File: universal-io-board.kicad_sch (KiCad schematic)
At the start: 34 parts, among them J1 Conn_01x03_Pin, J2 Conn_01x22_Socket, J3 Conn_01x22_Socket, J4 Conn_01x02, U1 R-78E5.0-1.0, U2 AMS1117-3.3, U3 ADS1256IDBT, U4 REF5050IDGK, Y1 Crystal

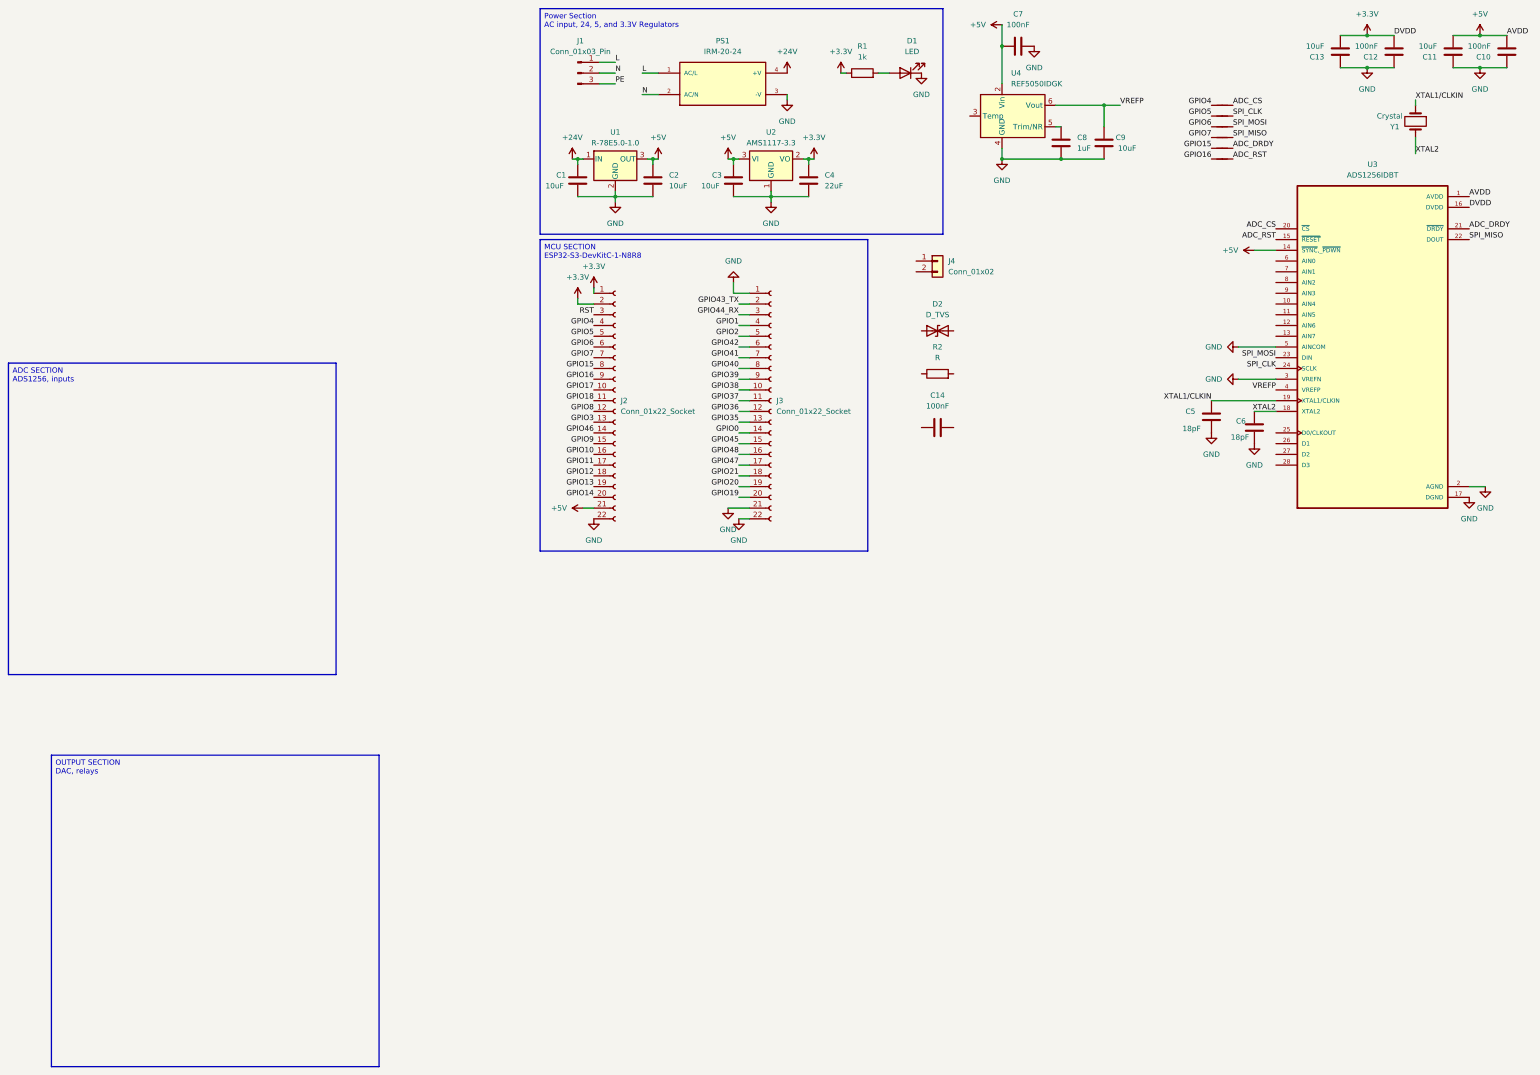
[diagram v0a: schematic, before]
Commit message: Updated schematic and PCB
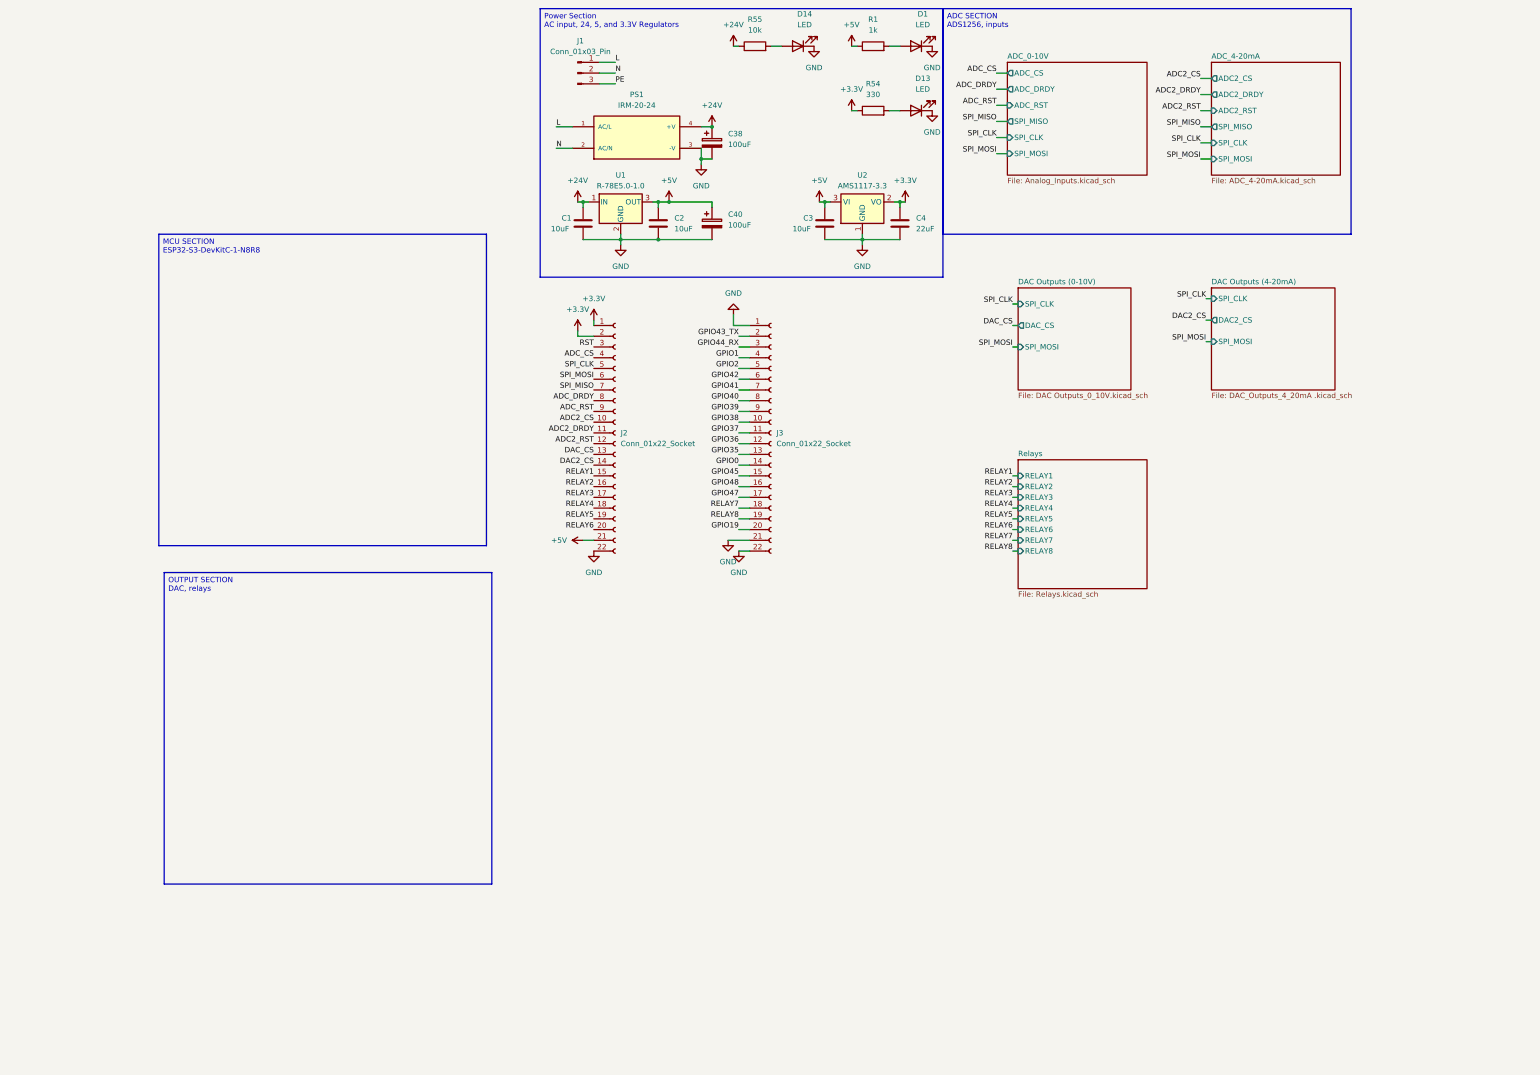
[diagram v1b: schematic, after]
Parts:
- removed C10, C12, C14, C7: 100nF, Capacitor_SMD:C_0805_2012Metric, symbol Device:C
- removed C11, C13, C9: 10uF, Capacitor_SMD:C_0805_2012Metric, symbol Device:C
- removed C5, C6: 18pF, Capacitor_SMD:C_0805_2012Metric, symbol Device:C
- removed C8: 1uF, Capacitor_SMD:C_0805_2012Metric, symbol Device:C
- removed D2: D_TVS, symbol Device:D_TVS
- removed J4: Conn_01x02, symbol Connector_Generic:Conn_01x02
- removed NT1, NT2, NT3, NT4, NT5, NT6: NetTie_2, symbol Device:NetTie_2
- removed R2: R, symbol Device:R
- removed U3: ADS1256IDBT, ADS1256IDBT:SOP65P780X200-28N, symbol ADS1256IDBT:ADS1256IDBT
- removed U4: REF5050IDGK, Package_SO:MSOP-8_3x3mm_P0.65mm, symbol Reference_Voltage:REF5050IDGK
- removed Y1: Crystal, Crystal:Crystal_SMD_HC49-SD, symbol Device:Crystal
- added C38, C40: 100uF, Capacitor_THT:CP_Radial_D6.3mm_P2.50mm, symbol Device:C_Polarized
- added D13, D14: LED, LED_SMD:LED_0805_2012Metric, symbol Device:LED
- added R54: 330, Resistor_SMD:R_0805_2012Metric, symbol Device:R
- added R55: 10k, Resistor_SMD:R_0805_2012Metric, symbol Device:R
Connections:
- net GPIO15 is gone; now on net ADC_DRDY: J2.8 (Pin_8)
- net GPIO16 is gone; now on net ADC_RST: J2.9 (Pin_9)
- net GPIO4 is gone; now on net ADC_CS: J2.4 (Pin_4)
- net GPIO5 is gone; now on net SPI_CLK: J2.5 (Pin_5)
- net GPIO6 is gone; now on net SPI_MOSI: J2.6 (Pin_6)
- net GPIO7 is gone; now on net SPI_MISO: J2.7 (Pin_7)
- net +24V: now also C38.1, R55.1
- net +3.3V: now also R54.1; no longer R1.1
- net +5V: now also R1.1, C40.1
- net GND: now also C38.2, C40.2, D13.1 (K), D14.1 (K)
- net GPIO10 renamed RELAY2
- net GPIO11 renamed RELAY3
- net GPIO12 renamed RELAY4
- net GPIO13 renamed RELAY5
- net GPIO14 renamed RELAY6
- net GPIO17 renamed ADC2_CS
- net GPIO18 renamed ADC2_DRDY
- net GPIO20 renamed RELAY8
- net GPIO21 renamed RELAY7
- net GPIO3 renamed DAC_CS
- net GPIO46 renamed DAC2_CS
- net GPIO8 renamed ADC2_RST
- net GPIO9 renamed RELAY1
- new net: D14.2 (A), R55.2
- new net: D13.2 (A), R54.2
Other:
- added sheet ADC_0-10V (Analog_Inputs.kicad_sch)
- added sheet ADC_4-20mA (ADC_4-20mA.kicad_sch)
- added sheet DAC Outputs (0-10V) (DAC Outputs_0_10V.kicad_sch)
- added sheet DAC Outputs (4-20mA) (DAC_Outputs_4_20mA .kicad_sch)
- added sheet Relays (Relays.kicad_sch)
- moved on the sheet: C1, C2, C3, C4, D1, J2, J3, PS1, R1, U1, U2

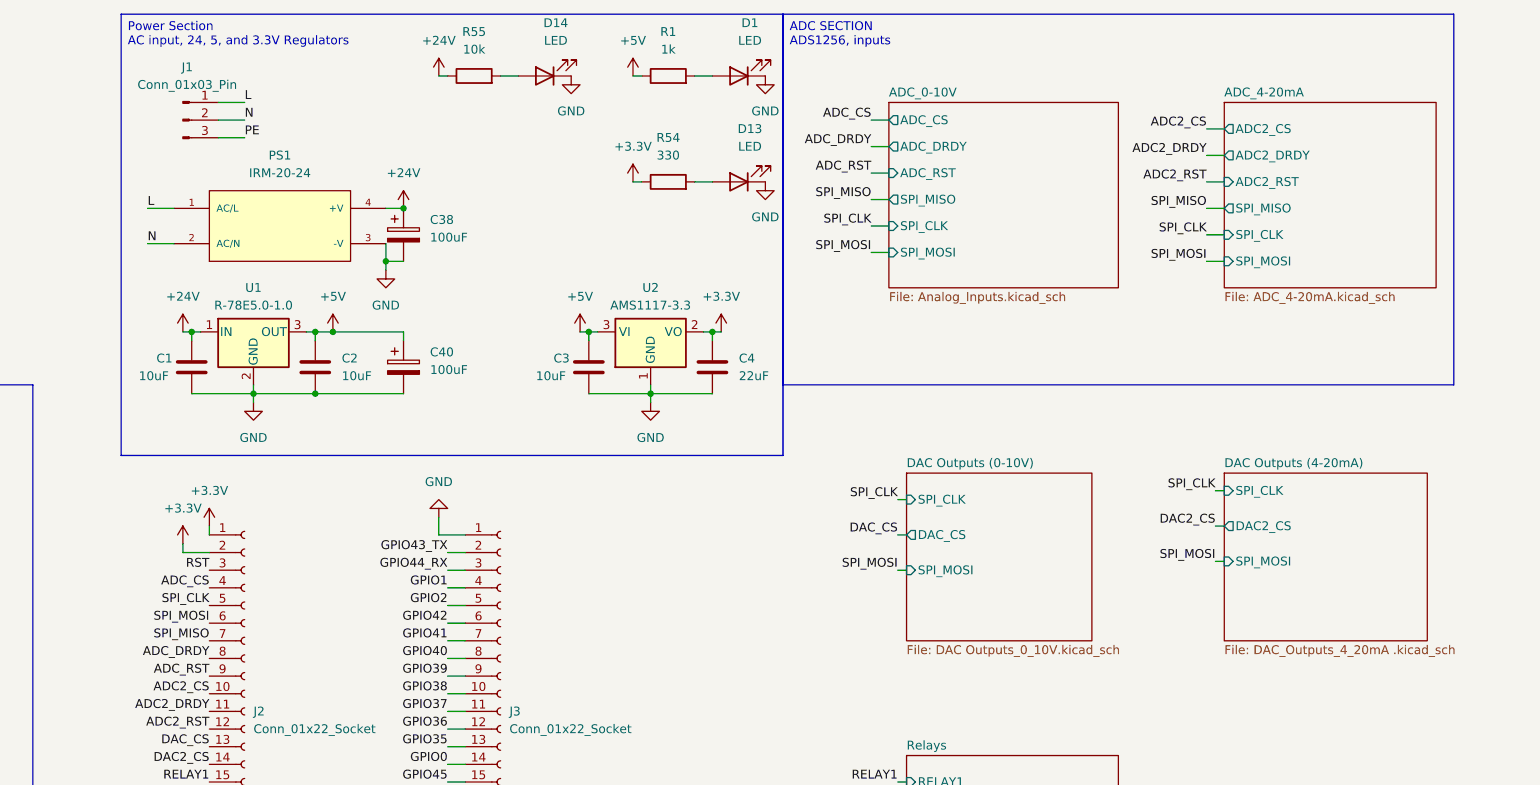
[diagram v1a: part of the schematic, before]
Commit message: Updated schematic and PCB
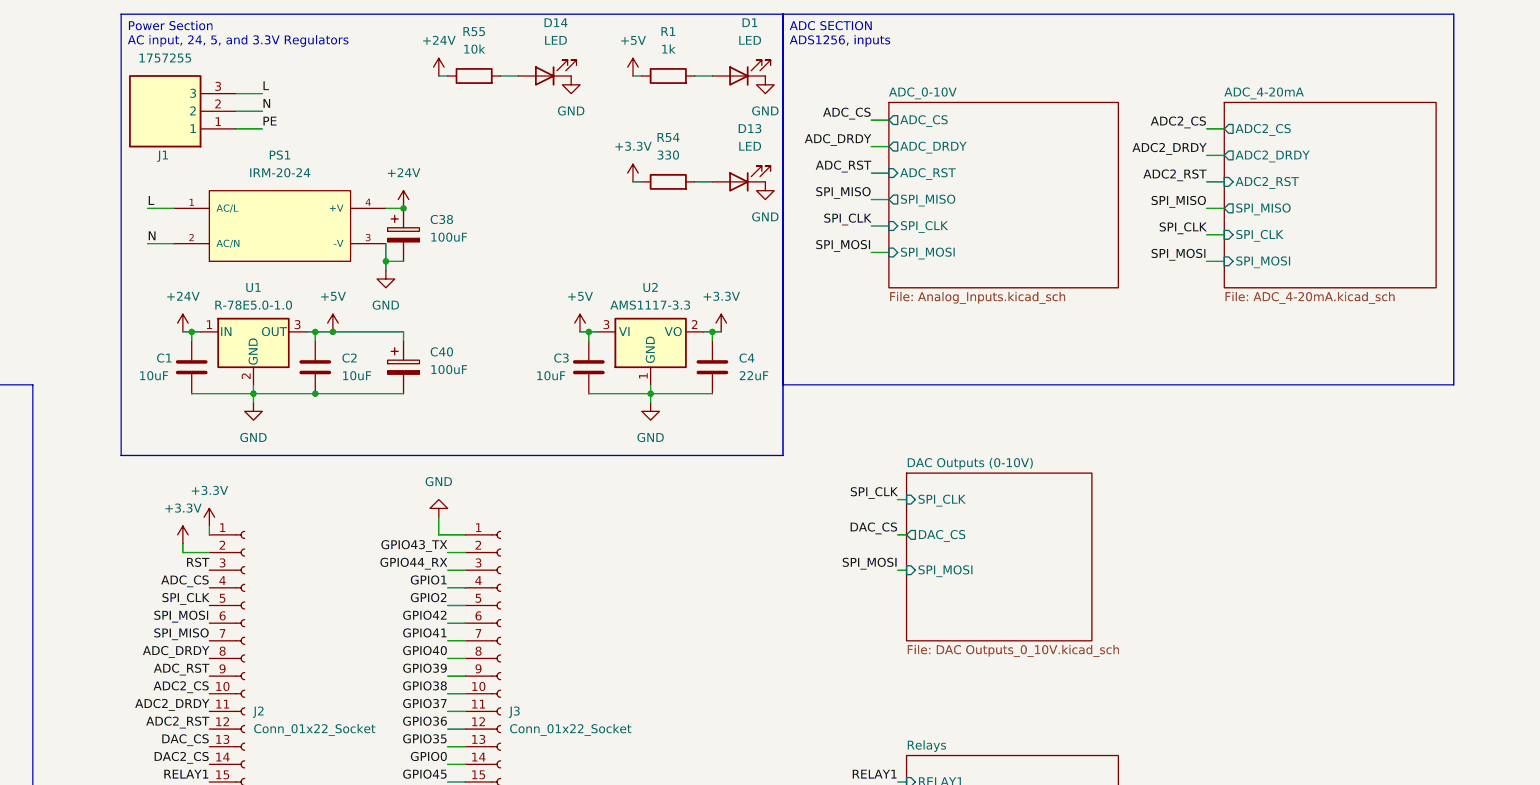
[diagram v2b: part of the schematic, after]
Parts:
- removed J1: Conn_01x03_Pin, 1715734:PHOENIX_1715734, symbol Connector:Conn_01x03_Pin
- added J1: 1757255, 1757255, symbol 1757255:1757255
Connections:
- net L: now also J1.3
- net N: now also J1.2
- net PE: now also J1.1
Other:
- removed sheet DAC Outputs (4-20mA)
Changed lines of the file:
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@@
 	(wire
 		(pts
-			(xy 170.18 86.36) (xy 171.45 86.36)
-		)
-		(stroke
-			(width 0)
-			(type default)
-		)
-	)
-	(wire
-		(pts
 			(xy 168.91 29.21) (xy 171.45 29.21)
 		)
@@
 	(wire
 		(pts
-			(xy 26.67 25.4) (xy 30.48 25.4)
-		)
-		(stroke
-			(width 0)
-			(type default)
-		)
-	)
-	(wire
-		(pts
-			(xy 170.18 81.28) (xy 171.45 81.28)
+			(xy 29.21 24.13) (xy 33.02 24.13)
 		)
 		(stroke
@@
 	(wire
 		(pts
-			(xy 26.67 27.94) (xy 30.48 27.94)
+			(xy 29.21 26.67) (xy 33.02 26.67)
 		)
 		(stroke
@@
 	(wire
 		(pts
-			(xy 26.67 30.48) (xy 30.48 30.48)
-		)
-		(stroke
-			(width 0)
-			(type default)
-		)
-	)
-	(wire
-		(pts
-			(xy 170.18 91.44) (xy 171.45 91.44)
+			(xy 29.21 29.21) (xy 33.02 29.21)
 		)
 		(stroke
@@
 	)
 	(label "PE"
-		(at 30.48 30.48 0)
+		(at 33.02 29.21 0)
 		(effects
 			(font
@@
 	)
 	(label "L"
-		(at 30.48 25.4 0)
+		(at 33.02 24.13 0)
 		(effects
 			(font
@@
 		)
 	)
-	(label "SPI_MOSI"
-		(at 170.18 91.44 180)
-		(effects
-			(font
-				(size 1.27 1.27)
-			)
-			(justify right bottom)
-		)
-	)
 	(label "ADC_DRDY"
 		(at 120.65 31.75 180)
@@
 		)
 	)
-	(label "DAC2_CS"
-		(at 170.18 86.36 180)
-		(effects
-			(font
-				(size 1.27 1.27)
-			)
-			(justify right bottom)
-		)
-	)
 	(label "RST"
 		(at 25.4 92.71 180)
@@
 	)
 	(label "N"
-		(at 30.48 27.94 0)
+		(at 33.02 26.67 0)
 		(effects
 			(font
@@
 	)
 	(label "SPI_CLK"
-		(at 170.18 81.28 180)
-		(effects
-			(font
-				(size 1.27 1.27)
-			)
-			(justify right bottom)
-		)
-	)
-	(label "SPI_CLK"
 		(at 120.65 43.18 180)
 		(effects
@@
 	)
 	(symbol
-		(lib_id "Connector:Conn_01x03_Pin")
-		(at 21.59 27.94 0)
-		(unit 1)
-		(exclude_from_sim no)
-		(in_bom yes)
-		(on_board yes)
-		(dnp no)
-		(fields_autoplaced yes)
-		(property "Reference" "J1"
-			(at 22.225 20.32 0)
-			(effects
-				(font
-					(size 1.27 1.27)
-				)
-			)
-		)
-		(property "Value" "Conn_01x03_Pin"
-			(at 22.225 22.86 0)
-			(effects
-				(font
-					(size 1.27 1.27)
-				)
-			)
-		)
-		(property "Footprint" "1715734:PHOENIX_1715734"
-			(at 21.59 27.94 0)
-			(effects
-				(font
-					(size 1.27 1.27)
-				)
-				(hide yes)
-			)
-		)
-		(property "Datasheet" "kicad-embed://phoenix-contact-1715734-en.pdf"
-			(at 21.59 27.94 0)
-			(effects
-				(font
-					(size 1.27 1.27)
-				)
-				(hide yes)
-			)
-		)
-		(property "Description" "Generic connector, single row, 01x03, script generated"
-			(at 21.59 27.94 0)
-			(effects
-				(font
-					(size 1.27 1.27)
-				)
-				(hide yes)
-			)
-		)
-		(pin "1"
-		)
-		(pin "3"
-		)
-		(pin "2"
-		)
-		(instances
-			(project ""
-				(path "/20540832-f0e7-4431-b65d-173d703fbd53"
-					(reference "J1")
-					(unit 1)
-				)
-			)
-		)
-	)
-	(symbol
 		(lib_id "Device:R")
 		(at 91.44 21.59 90)
@@
 		(on_board yes)
 		(dnp no)
-		(fields_autoplaced yes)
 		(property "Reference" "PS1"
 			(at 35.56 33.02 0)
@@
 	)
 	(symbol
+		(lib_id "1757255:1757255")
+		(at 29.21 29.21 180)
+		(unit 1)
+		(exclude_from_sim no)
+		(in_bom yes)
+		(on_board yes)
+		(dnp no)
+		(property "Reference" "J1"
+			(at 18.796 33.02 0)
+			(effects
+				(font
+					(size 1.27 1.27)
+				)
+			)
+		)
+		(property "Value" "1757255"
+			(at 19.05 19.05 0)
+			(effects
+				(font
+					(size 1.27 1.27)
+				)
+			)
+		)
+		(property "Footprint" "1757255"
+			(at 12.7 -65.71 0)
+			(effects
+				(font
+					(size 1.27 1.27)
+				)
+				(justify left top)
+				(hide yes)
+			)
+		)
+		(property "Datasheet" "https://www.phoenixcontact.com/en-us/products/pcb-header-mstba-25-3-g-508-1757255?type=pdf"
+			(at 12.7 -165.71 0)
+			(effects
+				(font
+					(size 1.27 1.27)
+				)
+				(justify left top)
+				(hide yes)
+			)
+		)
+		(property "Description" "PCB header, nominal cross section: 2.5 mm?, color: green, nominal current: 12 A, rated voltage (III/2): 320 V, contact surface: Tin, type of contact: Male connector, Number of potentials: 3, Number of rows: 1, Number of positions per row: 3, number of connections: 3, product range: MSTBA 2,5/..-G, pitch: 5.08 mm, mounting: Wave soldering, pin layout: Linear pinning, solder pin [P]: 3.5 mm, Stecksystem: CLASSIC COMBICON, Locking: without, type of packaging: packed in cardboard"
+			(at 29.21 29.21 0)
+			(effects
+				(font
+					(size 1.27 1.27)
+				)
+				(hide yes)
+			)
+		)
+		(property "Height" "8.72"
+			(at 12.7 -365.71 0)
+			(effects
+				(font
+					(size 1.27 1.27)
+				)
+				(justify left top)
+				(hide yes)
+			)
+		)
+		(property "Manufacturer_Name" "Phoenix Contact"
+			(at 12.7 -465.71 0)
+			(effects
+				(font
+					(size 1.27 1.27)
+				)
+				(justify left top)
+				(hide yes)
+			)
+		)
+		(property "Manufacturer_Part_Number" "1757255"
+			(at 12.7 -565.71 0)
+			(effects
+				(font
+					(size 1.27 1.27)
+				)
+				(justify left top)
+				(hide yes)
+			)
+		)
+		(property "Mouser Part Number" "651-1757255"
+			(at 12.7 -665.71 0)
+			(effects
+				(font
+					(size 1.27 1.27)
+				)
+				(justify left top)
+				(hide yes)
+			)
+		)
+		(property "Mouser Price/Stock" "https://www.mouser.co.uk/ProductDetail/Phoenix-Contact/1757255?qs=uD%2FdkN7XIa0ez8xszzicKg%3D%3D"
+			(at 12.7 -765.71 0)
+			(effects
+				(font
+					(size 1.27 1.27)
+				)
+				(justify left top)
+				(hide yes)
+			)
+		)
+		(property "Arrow Part Number" "1757255"
+			(at 12.7 -865.71 0)
+			(effects
+				(font
+					(size 1.27 1.27)
+				)
+				(justify left top)
+				(hide yes)
+			)
+		)
+		(property "Arrow Price/Stock" "https://www.arrow.com/en/products/1757255/phoenix-contact?utm_currency=USD&region=nac"
+			(at 12.7 -965.71 0)
+			(effects
+				(font
+					(size 1.27 1.27)
+				)
+				(justify left top)
+				(hide yes)
+			)
+		)
+		(pin "1"
+		)
+		(pin "3"
+		)
+		(pin "2"
+		)
+		(instances
+			(project ""
+				(path "/20540832-f0e7-4431-b65d-173d703fbd53"
+					(reference "J1")
+					(unit 1)
+				)
+			)
+		)
+	)
+	(symbol
 		(lib_id "power:+5V")
 		(at 22.86 138.43 90)
@@
 				)
 			)
-		)
-	)
-	(sheet
-		(at 171.45 78.74)
-		(size 29.21 24.13)
-		(exclude_from_sim no)
-		(in_bom yes)
-		(on_board yes)
-		(dnp no)
-		(fields_autoplaced yes)
-		(stroke
-			(width 0.1524)
-			(type solid)
-		)
-		(fill
-			(color 0 0 0 0.0000)
-		)
-		(property "Sheetname" "DAC Outputs (4-20mA)"
-			(at 171.45 78.0284 0)
-			(effects
-				(font
-					(size 1.27 1.27)
-				)
-				(justify left bottom)
-			)
-		)
-		(property "Sheetfile" "DAC_Outputs_4_20mA .kicad_sch"
-			(at 171.45 103.4546 0)
-			(effects
-				(font
-					(size 1.27 1.27)
-				)
-				(justify left top)
-			)
-		)
-		(pin "SPI_CLK" input
-			(at 171.45 81.28 180)
-			(effects
-				(font
-					(size 1.27 1.27)
-				)
-				(justify left)
-			)
-		)
-		(pin "SPI_MOSI" input
-			(at 171.45 91.44 180)
-			(effects
-				(font
-					(size 1.27 1.27)
-				)
-				(justify left)
-			)
-		)
-		(pin "DAC2_CS" output
-			(at 171.45 86.36 180)
-			(effects
-				(font
-					(size 1.27 1.27)
-				)
-				(justify left)
-			)
-		)
-		(instances
-			(project "universal-io-board"
-				(path "/20540832-f0e7-4431-b65d-173d703fbd53"
-					(page "5")
-				)
-			)
